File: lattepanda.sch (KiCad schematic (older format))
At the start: 5 parts

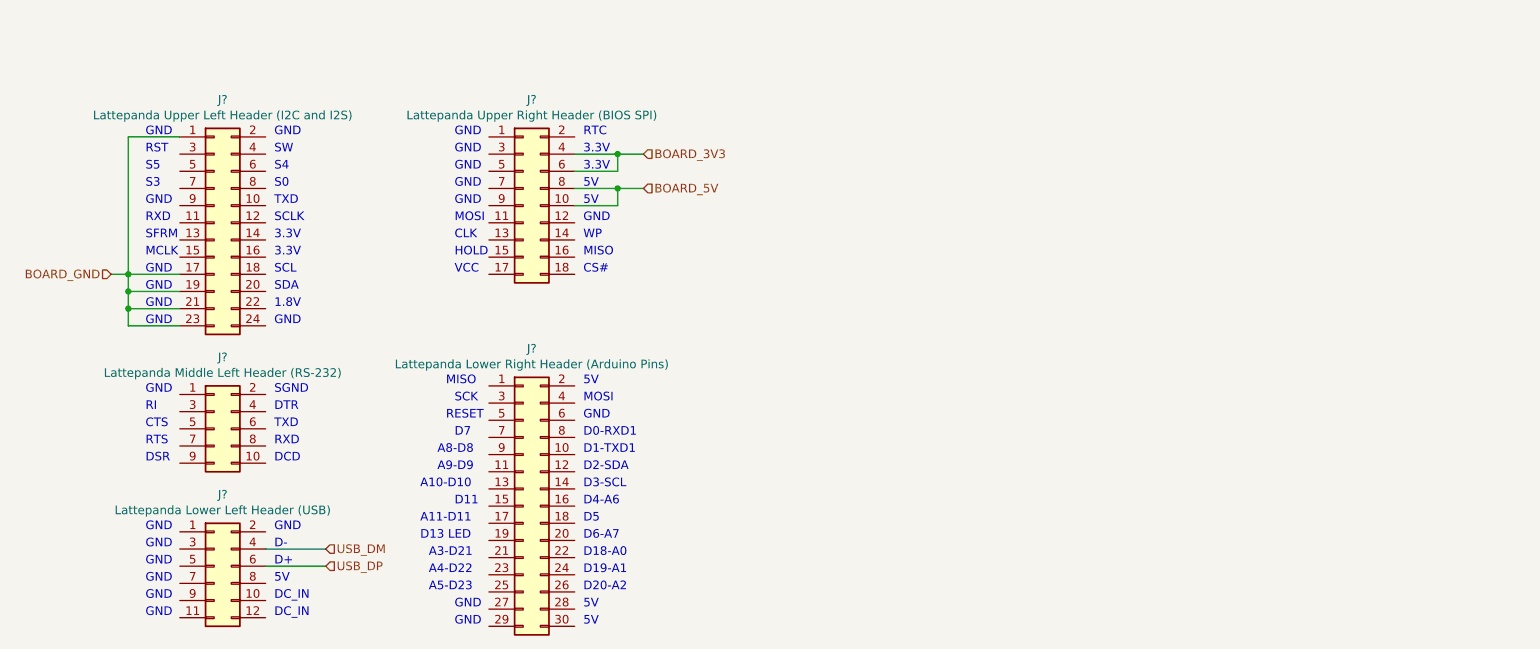
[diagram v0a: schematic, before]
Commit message: Added labels to all components
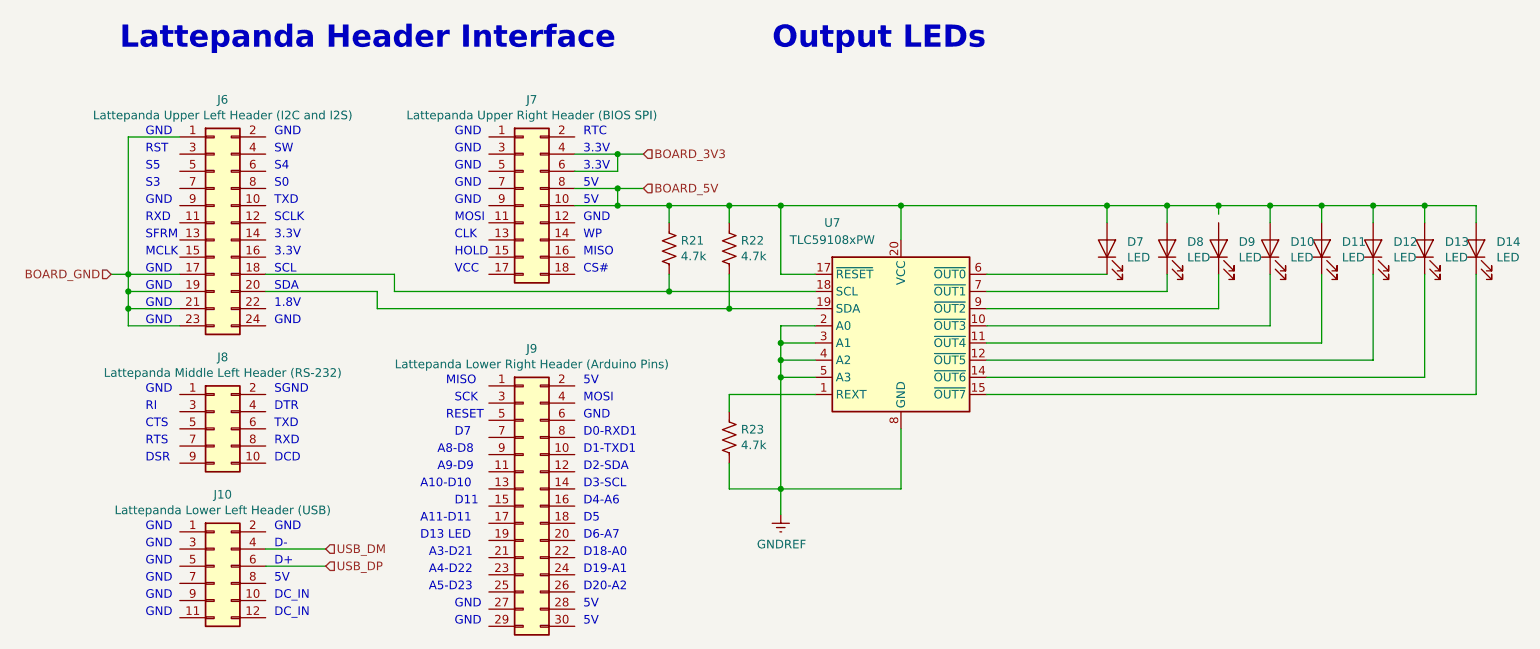
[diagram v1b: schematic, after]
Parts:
- added D10, D11, D12, D13, D14, D7, D8, D9: LED, symbol Device:LED
- added R21, R22, R23: 4.7k, symbol Device:R_US
- added U7: TLC59108xPW, Package_SO:TSSOP-20_4.4x6.5mm_P0.65mm, symbol Driver_LED:TLC59108xPW
- gave numbers to parts that had none: 5
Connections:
- net BOARD_5V: now also D10.2 (A), D11.2 (A), D12.2 (A), D13.2 (A), D14.2 (A), D7.2 (A), D8.2 (A), R21.1, R22.1, U7.17 (~RESET), U7.20 (VCC)
- net at J6.18 (Pin_18): now also R21.2, U7.18 (SCL)
- net at J6.20 (Pin_20): now also R22.2, U7.19 (SDA)
- new net: R23.1, U7.1 (REXT)
- new net: D10.1 (K), U7.10 (~OUT3)
- new net: D11.1 (K), U7.11 (~OUT4)
- new net: D12.1 (K), U7.12 (~OUT5)
- new net: D13.1 (K), U7.14 (~OUT6)
- new net: D14.1 (K), U7.15 (~OUT7)
- new net: D7.1 (K), U7.6 (~OUT0)
- new net: D8.1 (K), U7.7 (~OUT1)
- new net: D9.1 (K), U7.9 (~OUT2)
- new net GNDREF: R23.2, U7.13 (GND), U7.16 (GND), U7.2 (A0), U7.3 (A1), U7.4 (A2), U7.5 (A3), U7.8 (GND)
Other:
- note added: "Lattepanda Header Interface"
- note added: "Output LEDs"
